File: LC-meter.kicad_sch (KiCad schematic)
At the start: 39 parts, among them J1 ResetSW, J2 ICSP, J3 1RowDsp, J4 OscTest, J5 Display, J6 Backled, J7 Power, J8 L/C, J9 L/C Switch, K1 SIP-1A05D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

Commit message: 9-10-2024
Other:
- title: (none) -> LC meter
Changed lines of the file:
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@@
 	(generator_version "8.0")
 	(paper "A4")
+	(title_block
+		(title "LC meter")
+		(date "2024-10-09")
+		(rev "0.1")
+	)
 	(junction
 		(at 238.76 143.51)

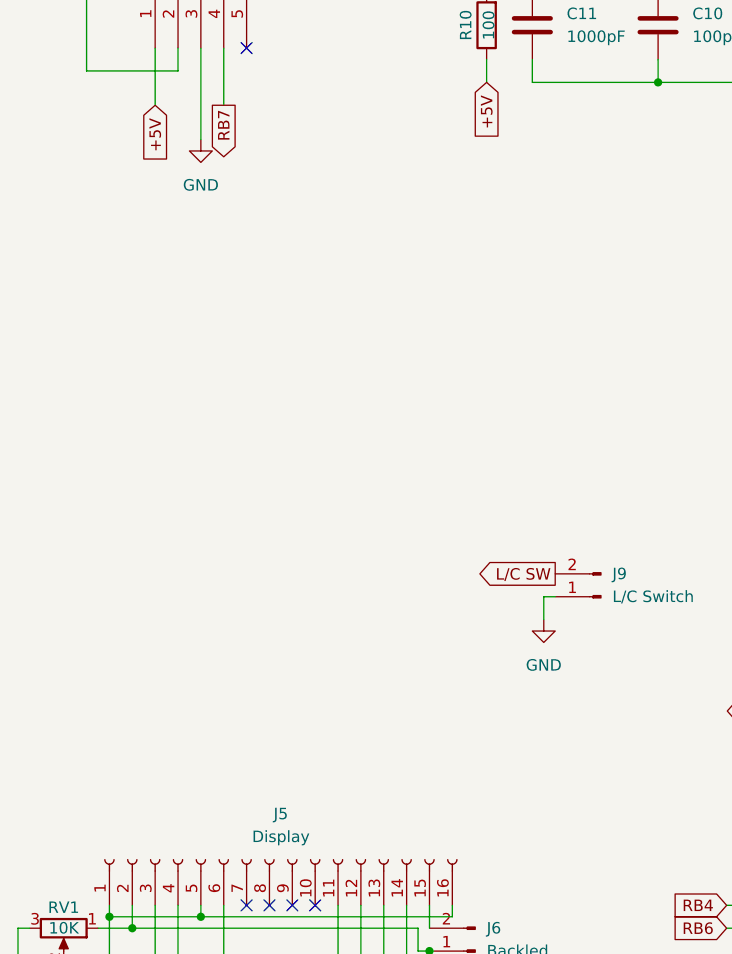
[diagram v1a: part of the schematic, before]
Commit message: add display
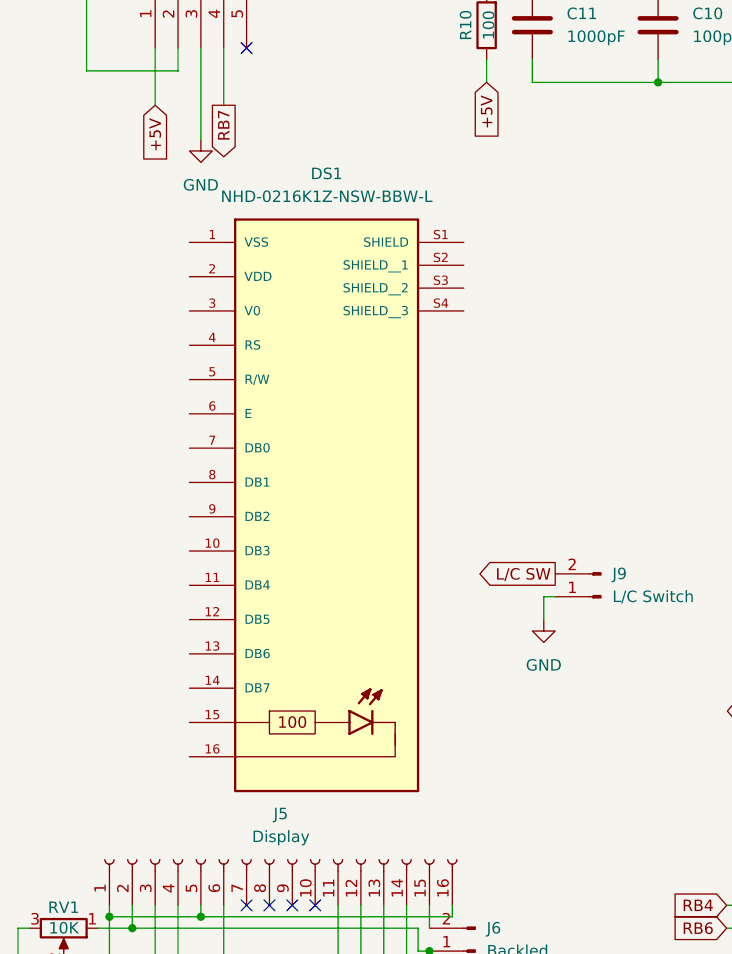
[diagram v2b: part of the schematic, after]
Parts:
- added DS1: NHD-0216K1Z-NSW-BBW-L, NHD-0216K1Z-NSW-BBW-L:NHD_NHD-0216K1Z-NSW-BBW-L, symbol NHD-0216K1Z-NSW-BBW-L:NHD-0216K1Z-NSW-BBW-L
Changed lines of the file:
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@@
+	)
+	(symbol
+		(lib_id "NHD-0216K1Z-NSW-BBW-L:NHD-0216K1Z-NSW-BBW-L")
+		(at 57.15 123.19 0)
+		(unit 1)
+		(exclude_from_sim yes)
+		(in_bom yes)
+		(on_board no)
+		(dnp no)
+		(fields_autoplaced yes)
+		(property "Reference" "DS1"
+			(at 57.15 97.79 0)
+			(effects
+				(font
+					(size 1.27 1.27)
+				)
+			)
+		)
+		(property "Value" "NHD-0216K1Z-NSW-BBW-L"
+			(at 57.15 100.33 0)
+			(effects
+				(font
+					(size 1.27 1.27)
+				)
+			)
+		)
+		(property "Footprint" "NHD-0216K1Z-NSW-BBW-L:NHD_NHD-0216K1Z-NSW-BBW-L"
+			(at 60.706 96.52 0)
+			(effects
+				(font
+					(size 1.27 1.27)
+				)
+				(justify bottom)
+				(hide yes)
+			)
+		)
+		(property "Datasheet" ""
+			(at 57.15 123.19 0)
+			(effects
+				(font
+					(size 1.27 1.27)
+				)
+				(hide yes)
+			)
+		)
+		(property "Description" ""
+			(at 57.15 123.19 0)
+			(effects
+				(font
+					(size 1.27 1.27)
+				)
+				(hide yes)
+			)
+		)
+		(property "PARTREV" "03/28/17"
+			(at 55.88 101.6 0)
+			(effects
+				(font
+					(size 1.27 1.27)
+				)
+				(justify bottom)
+				(hide yes)
+			)
+		)
+		(property "STANDARD" "Manufacturer Recommendations"
+			(at 21.59 118.11 0)
+			(effects
+				(font
+					(size 1.27 1.27)
+				)
+				(justify bottom)
+				(hide yes)
+			)
+		)
+		(property "MAXIMUM_PACKAGE_HEIGHT" "13.5mm"
+			(at 76.708 121.666 0)
+			(effects
+				(font
+					(size 1.27 1.27)
+				)
+				(justify bottom)
+				(hide yes)
+			)
+		)
+		(property "MANUFACTURER" "Newhaven Display International"
+			(at 83.82 127.762 0)
+			(effects
+				(font
+					(size 1.27 1.27)
+				)
+				(justify bottom)
+				(hide yes)
+			)
+		)
+		(pin "12"
+		)
+		(pin "11"
+		)
+		(pin "14"
+		)
+		(pin "10"
+		)
+		(pin "6"
+		)
+		(pin "16"
+		)
+		(pin "13"
+		)
+		(pin "8"
+		)
+		(pin "5"
+		)
+		(pin "1"
+		)
+		(pin "S4"
+		)
+		(pin "S2"
+		)
+		(pin "2"
+		)
+		(pin "9"
+		)
+		(pin "15"
+		)
+		(pin "3"
+		)
+		(pin "4"
+		)
+		(pin "7"
+		)
+		(pin "S3"
+		)
+		(pin "S1"
+		)
+		(instances
+			(project ""
+				(path "/acfd1337-269e-4290-80c6-927210c50877"
+					(reference "DS1")
+					(unit 1)
+				)
+			)
+		)
 	)
 	(symbol

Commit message: 11-10-2024
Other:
- moved on the sheet: DS1, J9
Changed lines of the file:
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@@
 	(wire
 		(pts
-			(xy 81.28 144.78) (xy 82.55 144.78)
+			(xy 149.86 123.19) (xy 151.13 123.19)
 		)
 		(stroke
@@
 	(wire
 		(pts
-			(xy 81.28 147.32) (xy 81.28 144.78)
+			(xy 149.86 125.73) (xy 149.86 123.19)
 		)
 		(stroke
@@
 	(global_label "L{slash}C SW"
 		(shape output)
-		(at 82.55 142.24 180)
+		(at 151.13 120.65 180)
 		(fields_autoplaced yes)
 		(effects
@@
 		)
 		(property "Intersheetrefs" "${INTERSHEET_REFS}"
-			(at 72.3077 142.24 0)
+			(at 140.8877 120.65 0)
 			(effects
 				(font
@@
 	(symbol
 		(lib_id "power:GND")
-		(at 81.28 147.32 0)
+		(at 149.86 125.73 0)
 		(unit 1)
 		(exclude_from_sim no)
@@
 		(fields_autoplaced yes)
 		(property "Reference" "#PWR013"
-			(at 81.28 153.67 0)
+			(at 149.86 132.08 0)
 			(effects
 				(font
@@
 		)
 		(property "Value" "GND"
-			(at 81.28 152.4 0)
+			(at 149.86 130.81 0)
 			(effects
 				(font
@@
 		)
 		(property "Footprint" ""
-			(at 81.28 147.32 0)
+			(at 149.86 125.73 0)
 			(effects
 				(font
@@
 		)
 		(property "Datasheet" ""
-			(at 81.28 147.32 0)
+			(at 149.86 125.73 0)
 			(effects
 				(font
@@
 		)
 		(property "Description" "Power symbol creates a global label with name \"GND\" , ground"
-			(at 81.28 147.32 0)
+			(at 149.86 125.73 0)
 			(effects
 				(font
@@
 	(symbol
 		(lib_id "NHD-0216K1Z-NSW-BBW-L:NHD-0216K1Z-NSW-BBW-L")
-		(at 57.15 123.19 0)
+		(at 74.93 124.46 0)
 		(unit 1)
 		(exclude_from_sim yes)
@@
 		(fields_autoplaced yes)
 		(property "Reference" "DS1"
-			(at 57.15 97.79 0)
+			(at 74.93 99.06 0)
 			(effects
 				(font
@@
 		)
 		(property "Value" "NHD-0216K1Z-NSW-BBW-L"
-			(at 57.15 100.33 0)
+			(at 74.93 101.6 0)
 			(effects
 				(font
@@
 		)
 		(property "Footprint" "NHD-0216K1Z-NSW-BBW-L:NHD_NHD-0216K1Z-NSW-BBW-L"
-			(at 60.706 96.52 0)
+			(at 78.486 97.79 0)
 			(effects
 				(font
@@
 		)
 		(property "Datasheet" ""
-			(at 57.15 123.19 0)
+			(at 74.93 124.46 0)
 			(effects
 				(font
@@
 		)
 		(property "Description" ""
-			(at 57.15 123.19 0)
+			(at 74.93 124.46 0)
 			(effects
 				(font
@@
 		)
 		(property "PARTREV" "03/28/17"
-			(at 55.88 101.6 0)
+			(at 73.66 102.87 0)
 			(effects
 				(font
@@
 		)
 		(property "STANDARD" "Manufacturer Recommendations"
-			(at 21.59 118.11 0)
+			(at 39.37 119.38 0)
 			(effects
 				(font
@@
 		)
 		(property "MAXIMUM_PACKAGE_HEIGHT" "13.5mm"
-			(at 76.708 121.666 0)
+			(at 94.488 122.936 0)
 			(effects
 				(font
@@
 		)
 		(property "MANUFACTURER" "Newhaven Display International"
-			(at 83.82 127.762 0)
+			(at 101.6 129.032 0)
 			(effects
 				(font
@@
 	(symbol
 		(lib_id "Connector:Conn_01x02_Pin")
-		(at 87.63 144.78 180)
+		(at 156.21 123.19 180)
 		(unit 1)
 		(exclude_from_sim no)
@@
 		(fields_autoplaced yes)
 		(property "Reference" "J9"
-			(at 88.9 142.2399 0)
+			(at 157.48 120.6499 0)
 			(effects
 				(font
@@
 		)
 		(property "Value" "L/C Switch"
-			(at 88.9 144.7799 0)
+			(at 157.48 123.1899 0)
 			(effects
 				(font
@@
 		)
 		(property "Footprint" "Connector_PinHeader_2.54mm:PinHeader_1x02_P2.54mm_Vertical"
-			(at 87.63 144.78 0)
+			(at 156.21 123.19 0)
 			(effects
 				(font
@@
 		)
 		(property "Datasheet" "~"
-			(at 87.63 144.78 0)
+			(at 156.21 123.19 0)
 			(effects
 				(font
@@
 		)
 		(property "Description" "Generic connector, single row, 01x02, script generated"
-			(at 87.63 144.78 0)
+			(at 156.21 123.19 0)
 			(effects
 				(font

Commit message: 11-10-2024 PCB ready
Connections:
- net GND: now also J4.1 (Pin_1); no longer J4.2 (Pin_2)
- net RB6: now also J4.2 (Pin_2); no longer J4.1 (Pin_1)
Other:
- moved on the sheet: J4
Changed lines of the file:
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@@
 	(symbol
 		(lib_id "Connector:Conn_01x02_Pin")
-		(at 106.68 186.69 90)
+		(at 109.22 186.69 270)
+		(mirror x)
 		(unit 1)
 		(exclude_from_sim no)
@@
 		(on_board yes)
 		(dnp no)
-		(fields_autoplaced yes)
 		(property "Reference" "J4"
-			(at 110.49 184.7849 90)
+			(at 105.41 184.7849 90)
 			(effects
 				(font
@@
 		)
 		(property "Value" "OscTest"
-			(at 110.49 187.3249 90)
+			(at 105.41 187.3249 90)
 			(effects
 				(font
@@
 		)
 		(property "Footprint" "Connector_PinHeader_2.54mm:PinHeader_1x02_P2.54mm_Vertical"
-			(at 106.68 186.69 0)
+			(at 109.22 186.69 0)
 			(effects
 				(font
@@
 		)
 		(property "Datasheet" "~"
-			(at 106.68 186.69 0)
+			(at 109.22 186.69 0)
 			(effects
 				(font
@@
 		)
 		(property "Description" "Generic connector, single row, 01x02, script generated"
-			(at 106.68 186.69 0)
+			(at 109.22 186.69 0)
 			(effects
 				(font

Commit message: Update 23-10-2024
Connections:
- net at U3.5 (BAL): now also U3.6 (STRB)
- no-connect marks 10 -> 8
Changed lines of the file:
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@@
-	)
-	(no_connect
-		(at 139.7 50.8)
 	)
 	(no_connect
@@
 		(at 48.26 48.26)
 	)
-	(no_connect
-		(at 137.16 50.8)
-	)
 	(wire
 		(pts
@@
 	(wire
 		(pts
+			(xy 137.16 50.8) (xy 139.7 50.8)
+		)
+		(stroke
+			(width 0)
+			(type default)
+		)
+	)
+	(wire
+		(pts
 			(xy 38.1 83.82) (xy 38.1 90.17)
 		)
@@
 		)
 	)
+	(text_box "RA0 ->\nRA1 -> 0 = \"energise relay\"\nRA2 -> Display \"E\"\nRA3 -> Display \"RS\"\nRA4 <- Counter in\nRB0 -> Display \"DB4\"\nRB1 -> Display \"DB5\"\nRB2 -> Display \"DB6\"\nRB3 -> Display \"DB7\"\nRB4 <- 0 = \"fix bad display\"\nRB5 <- Nc\nRB6 <- 0 = \"Setup\"\nRB7 <- 0 = \"Inductor\""
+		(exclude_from_sim no)
+		(at 195.58 96.52 0)
+		(size 78.74 31.75)
+		(stroke
+			(width 0)
+			(type default)
+		)
+		(fill
+			(type none)
+		)
+		(effects
+			(font
+				(size 1.27 1.27)
+			)
+			(justify left top)
+		)
+	)
